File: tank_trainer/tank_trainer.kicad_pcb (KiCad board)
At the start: 2 copper layers, 37.7 x 52.9 mm, 27 parts, among them U1 L7805, U2 ATMEGA328P-PU, Y1 Crystal

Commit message: Tank Trainer: Fix for capacitor location
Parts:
- moved C6 16.2 mm to (53.0, 87.0), turned to 90 degrees
- moved C5 13.9 mm to (53.0, 103.0), turned to 180 degrees
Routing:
- net Net-(U2-(PCINT14/~{RESET})PC6): track 34.6 -> 16.5 mm
- net Net-(ProgrammingHeader1-Pin_6): track 16.6 -> 3.52 mm
- net Net-(U2-(PCINT7/XTAL2/TOSC2)PB7): track 28.2 -> 16.0 mm
- net GND: track 132.9 -> 133.7 mm
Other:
- board text added: "Laser Tag Robot Tank Tank Trainer v0.4"
- board text removed: "Laser Tag Robot Tank Tank Trainer v0.3"

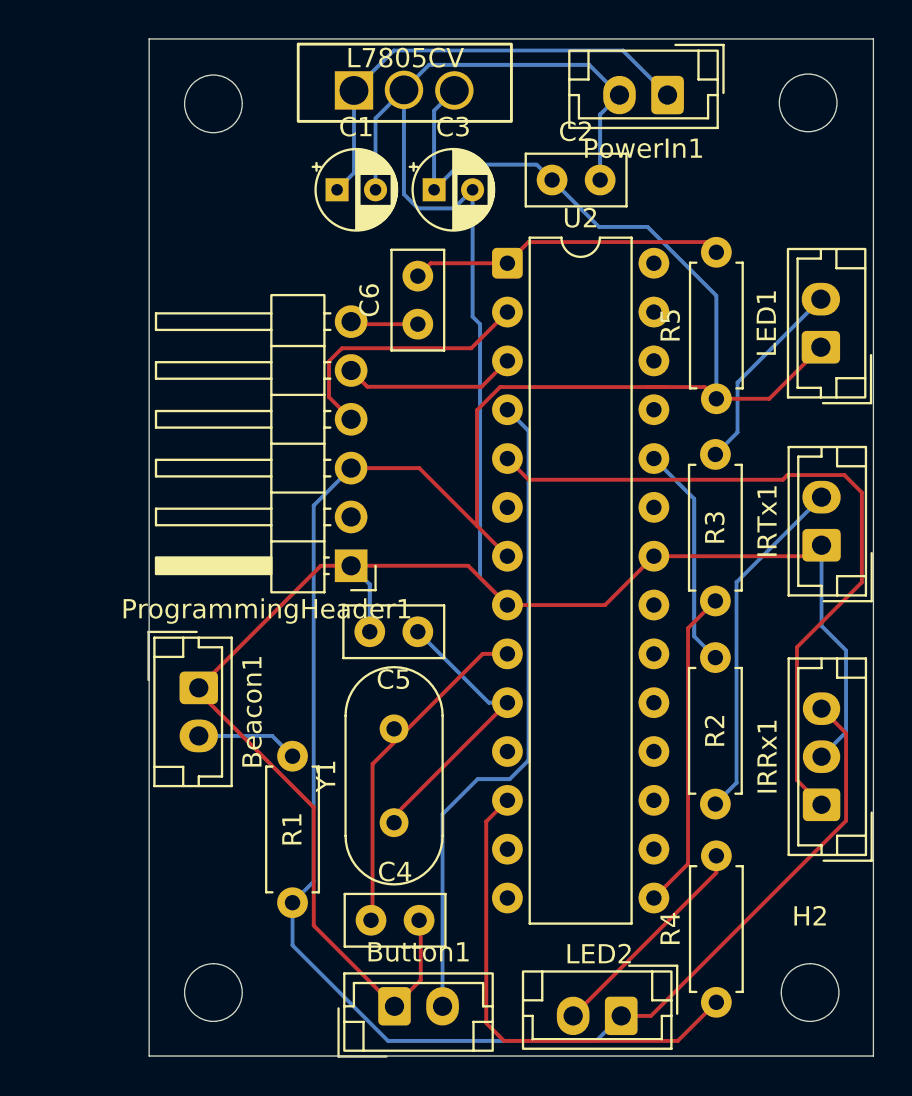
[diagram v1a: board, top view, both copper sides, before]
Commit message: Tank Trainer updates - LED1 is always-on
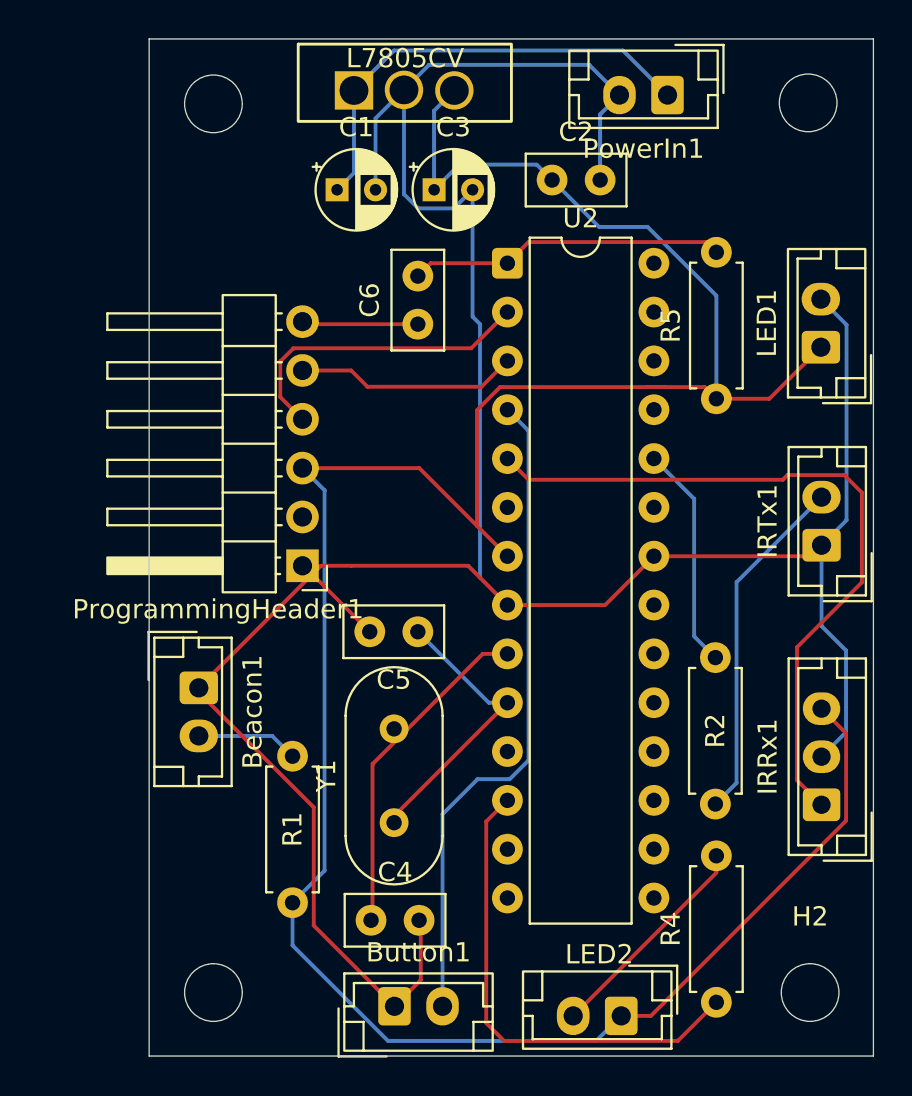
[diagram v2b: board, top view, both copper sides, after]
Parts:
- removed G***: LOGO, custom:Tank
- removed R3: R, Resistor_THT:R_Axial_DIN0207_L6.3mm_D2.5mm_P7.62mm_Horizontal
- moved ProgrammingHeader1 2.53 mm to (47.0, 99.6)
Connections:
- LED1 pad 2: Net-(LED1-Pin_2) -> GND
- U2 pad 15: Net-(U2-(PCINT1/OC1A)PB1) -> unconnected-(U2-(PCINT1/OC1A)PB1-Pad15)
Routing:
- net Net-(U2-(PCINT1/OC1A)PB1): track 16.8 -> 0.00 mm
- net GND: track 133.7 -> 148.7 mm
- net Net-(LED1-Pin_2): track 10.3 -> 0.00 mm
- net Rx: track 13.8 -> 16.4 mm
- net Net-(ProgrammingHeader1-Pin_6): track 3.52 -> 6.05 mm
- net Tx: track 9.04 -> 11.6 mm
- net 4.5V: track 134.7 -> 137.1 mm
